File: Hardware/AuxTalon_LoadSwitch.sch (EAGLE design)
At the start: 64 parts, among them J1 CONN_AUX_M12_REMOTE, J2 CONN_AUX_M12_REMOTE, J3 CONN_AUX_M12_REMOTE, J4 CONN_TALON_REMOTE, U1 ADS1115, U11 MCP23018QFN, U16 MAX9064, U17 MAX9064, U18 SN74AUP1T87, U19 MAX9064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

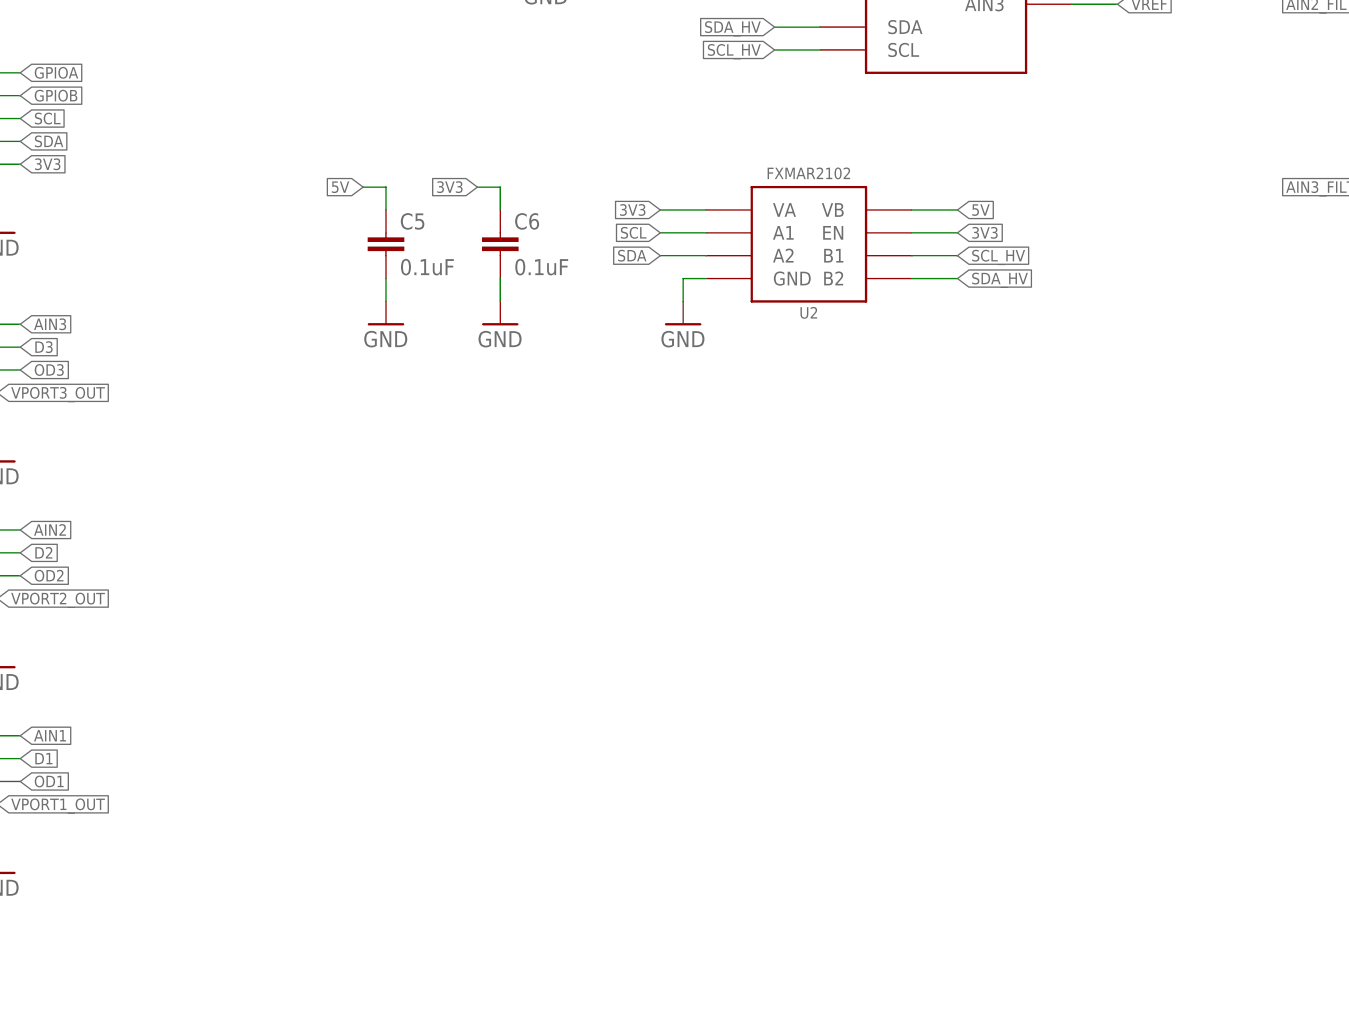
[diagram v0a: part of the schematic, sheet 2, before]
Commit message: Added ESD diodes, moved connector positioning
Added some ESD diodes on signal lines and changed positioning of connectors to restrict install to a single direction
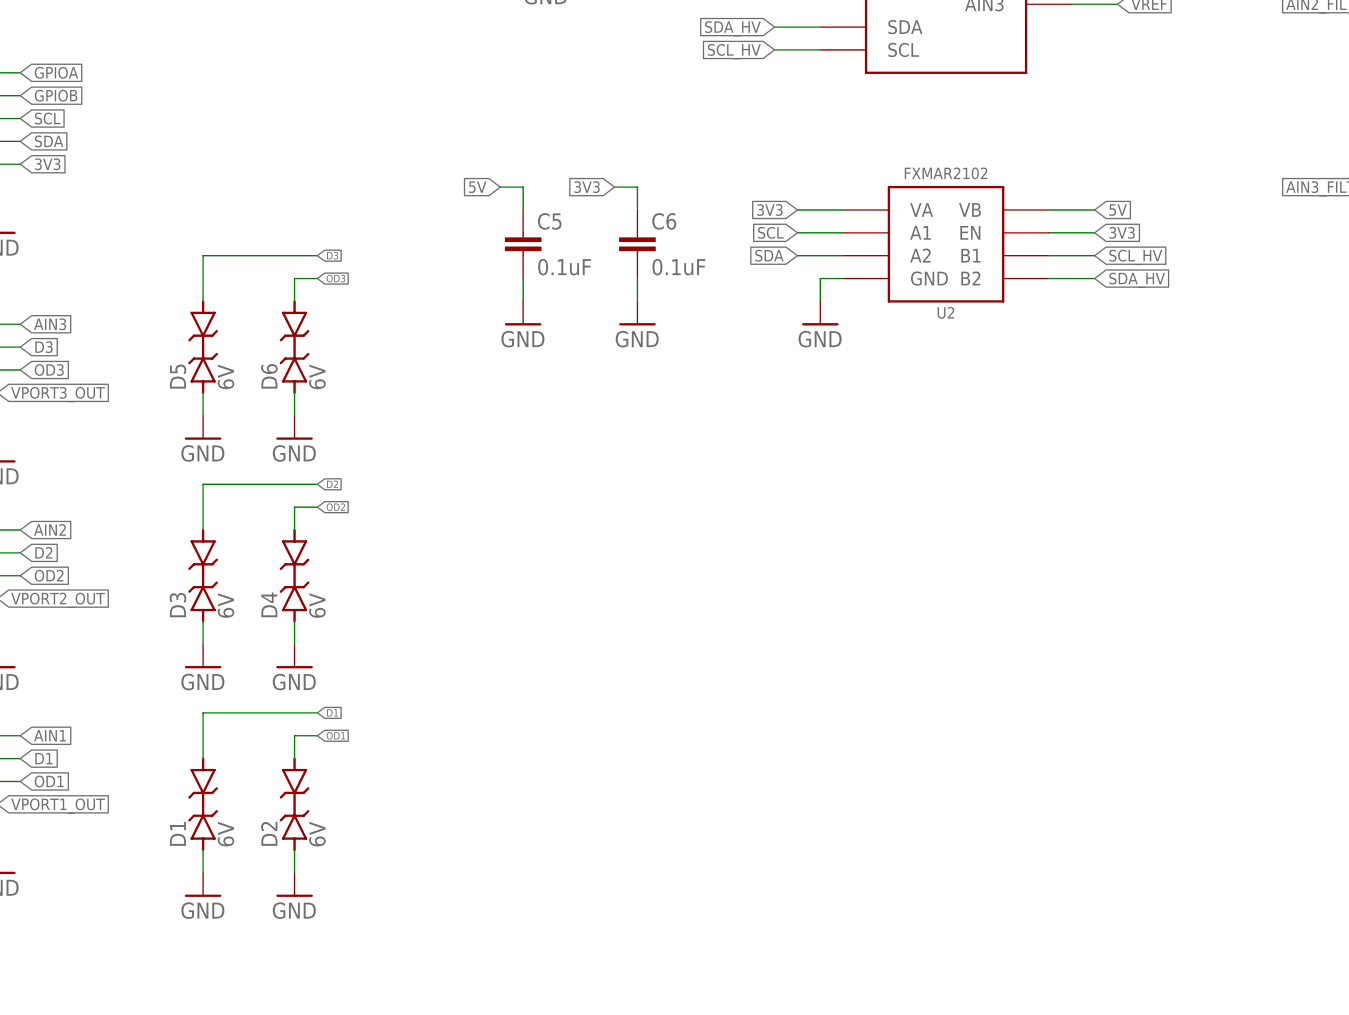
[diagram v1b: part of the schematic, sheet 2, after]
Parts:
- added D1, D2, D3, D4, D5, D6: 6V, bschulz:DIODE_ESD_BI_D5V0L1_0402
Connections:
- net D1: now also D1.C
- net D2: now also D3.C
- net D3: now also D5.C
- net GND: now also D1.A, D2.A, D3.A, D4.A, D5.A, D6.A
- net OD1: now also D2.C
- net OD2: now also D4.C
- net OD3: now also D6.C
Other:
- moved on the sheet: C5, C6, U2

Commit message: Layout, gerbers, and BoM for v0.0 - sent to fab
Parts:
- C10, C9: DIGIKEY (none) -> 732-6423-1-ND; MF (none) -> Wurth; MPN (none) -> 875105344008
- L1: DIGIKEY (none) -> 732-1012-1-ND; MF (none) -> Wurth; MPN (none) -> 744031220
- R14, R20: value (none) -> 82k; device bschulz_passives:R-EU_R0603 -> bschulz_passives:R-EU_82KR0603
- R15, R19: value (none) -> 62k; device bschulz_passives:R-EU_R0603 -> bschulz_passives:R-EU_62KR0603
- R21: value (none) -> 10k; device bschulz_passives:R-EU_R0603 -> bschulz_passives:R-EU_10KR0603
- R22: value (none) -> 150k; device bschulz_passives:R-EU_R0603 -> bschulz_passives:R-EU_150KR0603
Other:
- note added: "ADR: 0x20"
- note added: "ADR: 0x23"
- note added: "ADR: 0x24"
- moved on the sheet: R19, R20, R21, R22, U25, U26

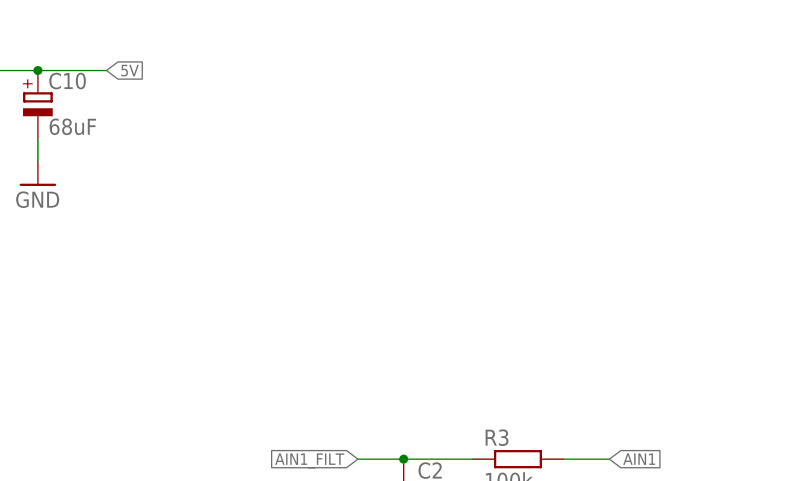
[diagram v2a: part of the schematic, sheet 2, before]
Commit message: v0.1 Updates - Added EEPROM
Added EEPROM to board
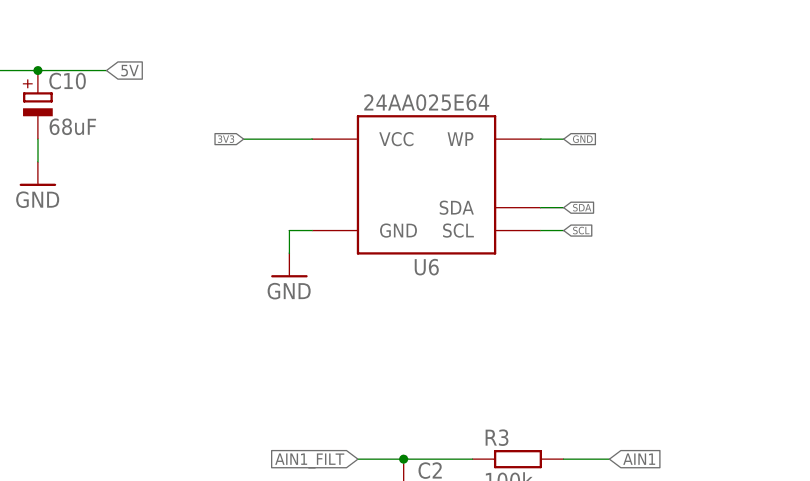
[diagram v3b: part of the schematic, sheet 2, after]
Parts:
- added U6: 24AA02SOT23, bschulz:24AA02SOT23
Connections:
- net 3V3: now also U6.VCC
- net GND: now also U6.GND, U6.WP
- net SCL: now also U6.SCL
- net SDA: now also U6.SDA
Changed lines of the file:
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@@
 <layer number="128" name="_bValues" color="7" fill="1" visible="no" active="yes"/>
 <layer number="129" name="Mask" color="7" fill="1" visible="no" active="yes"/>
+<layer number="130" name="SMDSTROOK" color="7" fill="1" visible="no" active="yes"/>
 <layer number="131" name="tAdjust" color="7" fill="1" visible="no" active="yes"/>
 <layer number="132" name="bAdjust" color="7" fill="1" visible="no" active="yes"/>
+<layer number="133" name="bottom_silk" color="7" fill="1" visible="no" active="yes"/>
+<layer number="134" name="mbFinish" color="7" fill="1" visible="no" active="no"/>
+<layer number="135" name="mtGlue" color="7" fill="1" visible="no" active="no"/>
+<layer number="136" name="mbGlue" color="7" fill="1" visible="no" active="no"/>
+<layer number="137" name="mtTest" color="7" fill="1" visible="no" active="no"/>
+<layer number="138" name="mbTest" color="7" fill="1" visible="no" active="no"/>
+<layer number="139" name="mtKeepout" color="7" fill="1" visible="no" active="no"/>
+<layer number="140" name="mbKeepout" color="7" fill="1" visible="no" active="no"/>
+<layer number="141" name="mtRestrict" color="7" fill="1" visible="no" active="no"/>
+<layer number="142" name="mbRestrict" color="7" fill="1" visible="no" active="no"/>
+<layer number="143" name="mvRestrict" color="7" fill="1" visible="no" active="no"/>
 <layer number="144" name="Drill_legend" color="7" fill="1" visible="no" active="yes"/>
+<layer number="145" name="mHoles" color="7" fill="1" visible="no" active="no"/>
+<layer number="146" name="mMilling" color="7" fill="1" visible="no" active="no"/>
+<layer number="147" name="mMeasures" color="7" fill="1" visible="no" active="no"/>
+<layer number="148" name="mDocument" color="7" fill="1" visible="no" active="no"/>
+<layer number="149" name="mReference" color="7" fill="1" visible="no" active="no"/>
 <layer number="150" name="Notes" color="7" fill="1" visible="no" active="yes"/>
 <layer number="151" name="HeatSink" color="7" fill="1" visible="no" active="yes"/>
@@
 <layer number="154" name="FabDoc2" color="7" fill="1" visible="no" active="yes"/>
 <layer number="155" name="FabDoc3" color="7" fill="1" visible="no" active="yes"/>
+<layer number="166" name="AntennaArea" color="7" fill="1" visible="no" active="yes"/>
+<layer number="168" name="4mmHeightArea" color="7" fill="1" visible="no" active="yes"/>
+<layer number="191" name="mNets" color="7" fill="1" visible="no" active="no"/>
+<layer number="192" name="mBusses" color="7" fill="1" visible="no" active="no"/>
+<layer number="193" name="mPins" color="7" fill="1" visible="no" active="no"/>
+<layer number="194" name="mSymbols" color="7" fill="1" visible="no" active="no"/>
+<layer number="195" name="mNames" color="7" fill="1" visible="no" active="no"/>
+<layer number="196" name="mValues" color="7" fill="1" visible="no" active="no"/>
 <layer number="199" name="Contour" color="7" fill="1" visible="no" active="yes"/>
 <layer number="200" name="200bmp" color="7" fill="1" visible="no" active="yes"/>
@@
 <part name="GND22" library="supply1" library_urn="urn:adsk.eagle:library:371" deviceset="GND" device=""/>
 <part name="GND23" library="supply1" library_urn="urn:adsk.eagle:library:371" deviceset="GND" device=""/>
+<part name="U6" library="bschulz" deviceset="24AA02" device="SOT23"/>
+<part name="GND24" library="supply1" library_urn="urn:adsk.eagle:library:371" deviceset="GND" device=""/>
 </parts>
 <sheets>
@@
 <attribute name="VALUE" x="63.5" y="15.24" size="1.778" layer="96"/>
 </instance>
+<instance part="U6" gate="G$1" x="193.04" y="167.64" smashed="yes">
+<attribute name="DISP" x="193.04" y="176.784" size="1.778" layer="95" ratio="15" align="center"/>
+<attribute name="NAME" x="193.04" y="158.496" size="1.778" layer="95" ratio="15" align="center"/>
+</instance>
+<instance part="GND24" gate="1" x="177.8" y="157.48" smashed="yes">
+<attribute name="VALUE" x="175.26" y="154.94" size="1.778" layer="96"/>
+</instance>
 </instances>
 <busses>
@@
 <wire x1="66.04" y1="71.12" x2="66.04" y2="73.66" width="0.1524" layer="91"/>
 </segment>
+<segment>
+<pinref part="U6" gate="G$1" pin="WP"/>
+<wire x1="205.74" y1="172.72" x2="208.28" y2="172.72" width="0.1524" layer="91"/>
+<label x="208.28" y="172.72" size="0.8128" layer="95" xref="yes"/>
+</segment>
+<segment>
+<pinref part="U6" gate="G$1" pin="GND"/>
+<wire x1="180.34" y1="162.56" x2="177.8" y2="162.56" width="0.1524" layer="91"/>
+<wire x1="177.8" y1="162.56" x2="177.8" y2="160.02" width="0.1524" layer="91"/>
+<pinref part="GND24" gate="1" pin="GND"/>
+</segment>
 </net>
 <net name="ADC_INT" class="0">
@@
 <label x="121.92" y="88.9" size="1.27" layer="95" rot="R180" xref="yes"/>
 </segment>
+<segment>
+<pinref part="U6" gate="G$1" pin="SDA"/>
+<wire x1="205.74" y1="165.1" x2="208.28" y2="165.1" width="0.1524" layer="91"/>
+<label x="208.28" y="165.1" size="0.8128" layer="95" xref="yes"/>
+</segment>
 </net>
 <net name="SCL" class="0">
@@
 <wire x1="127" y1="91.44" x2="121.92" y2="91.44" width="0.1524" layer="91"/>
 <label x="121.92" y="91.44" size="1.27" layer="95" rot="R180" xref="yes"/>
+</segment>
+<segment>
+<pinref part="U6" gate="G$1" pin="SCL"/>
+<wire x1="205.74" y1="162.56" x2="208.28" y2="162.56" width="0.1524" layer="91"/>
+<label x="208.28" y="162.56" size="0.8128" layer="95" xref="yes"/>
 </segment>
 </net>
@@
 <label x="203.2" y="22.86" size="1.27" layer="95" rot="R180" xref="yes"/>
 </segment>
+<segment>
+<pinref part="U6" gate="G$1" pin="VCC"/>
+<wire x1="180.34" y1="172.72" x2="172.72" y2="172.72" width="0.1524" layer="91"/>
+<label x="172.72" y="172.72" size="0.8128" layer="95" rot="R180" xref="yes"/>
+</segment>
 </net>
